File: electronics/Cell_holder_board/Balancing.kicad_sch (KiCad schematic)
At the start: 20 parts, among them Q1 IRLB8721PBF, Q2 IRLB8721PBF, Q3 IRLB8721PBF, Q4 IRLB8721PBF, U3 LTV-817, U4 LTV-817, U5 LTV-817, U6 LTV-817

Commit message: discord session with Johannes and Fabian, Schematic nearly done, all footprints fields filled
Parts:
- removed R17, R18, R19: 100, Resistor_THT:R_Axial_DIN0207_L6.3mm_D2.5mm_P10.16mm_Horizontal, symbol Device:R
- added R20 (x7): 100, Resistor_THT:R_Axial_DIN0207_L6.3mm_D2.5mm_P10.16mm_Horizontal, symbol Device:R
- R21, R22, R23, R24, R25, R26, R27, R28: footprint Resistor_THT:R_Axial_DIN0207_L6.3mm_D2.5mm_P10.16mm_Horizontal -> Resistor_SMD:R_0805_2012Metric
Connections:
- net BT1_+/BT2_-: now also R20.1
- net BT2_+/BT3_-: now also R20.1, R20.1
- net BT3_+/BT4_-: now also R20.1, R20.1
- net BT4_+: now also R20.1, R20.1
- net at Q4.2 (D), R20.2: now also R20.2
- net at Q2.2 (D): now also R20.2, R20.2
- net at Q3.2 (D): now also R20.2, R20.2
- net at Q1.2 (D): now also R20.2, R20.2

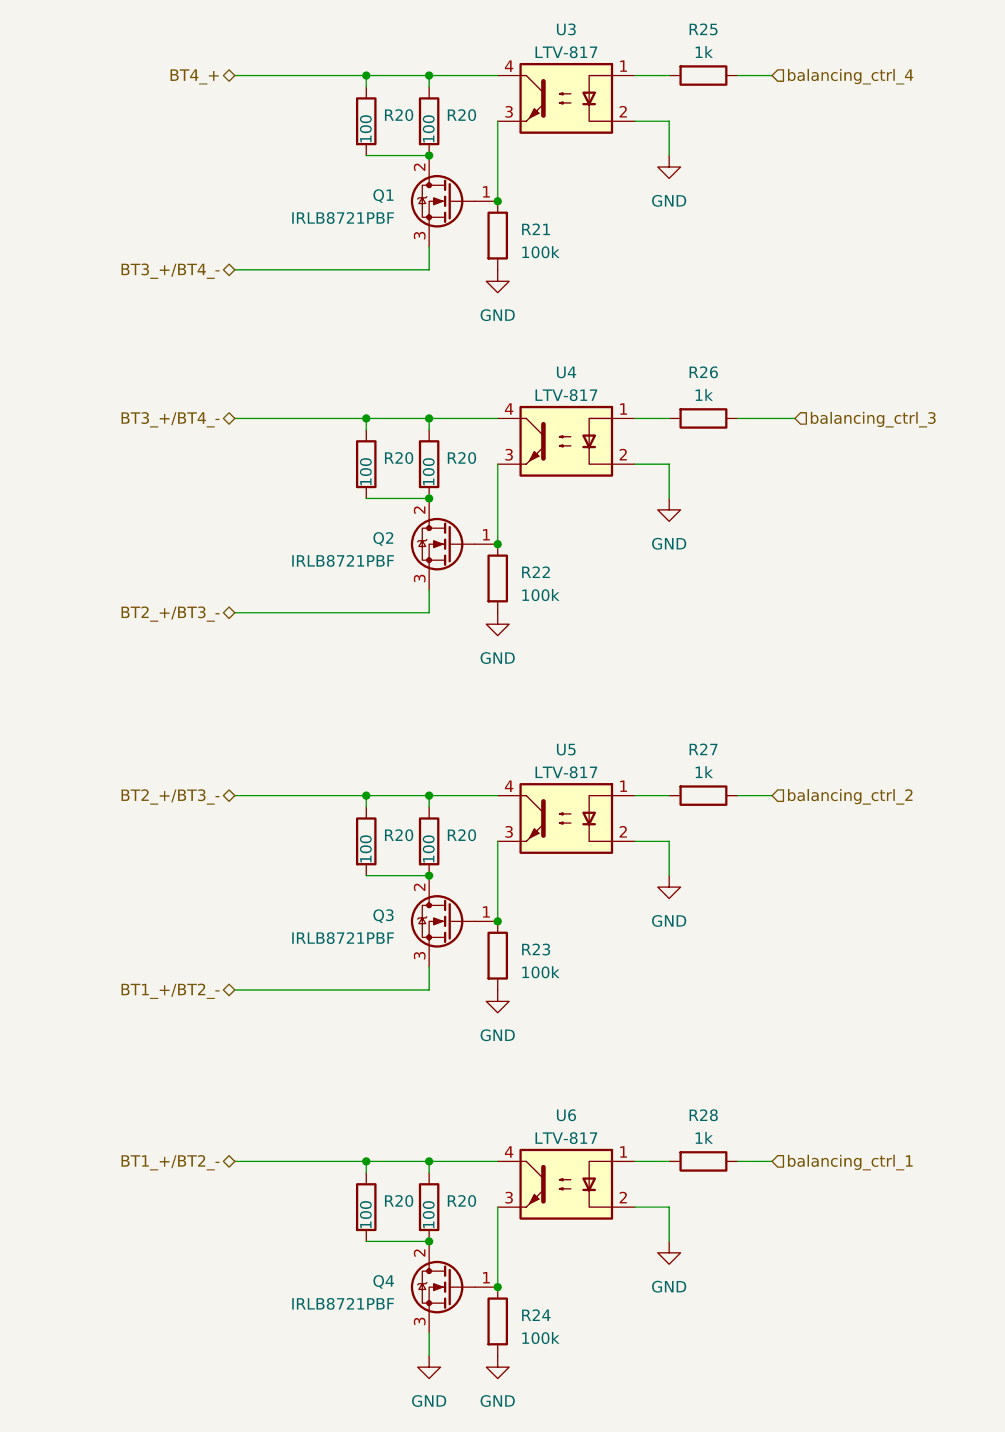
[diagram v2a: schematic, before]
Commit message: finished layout of cell_holder_board
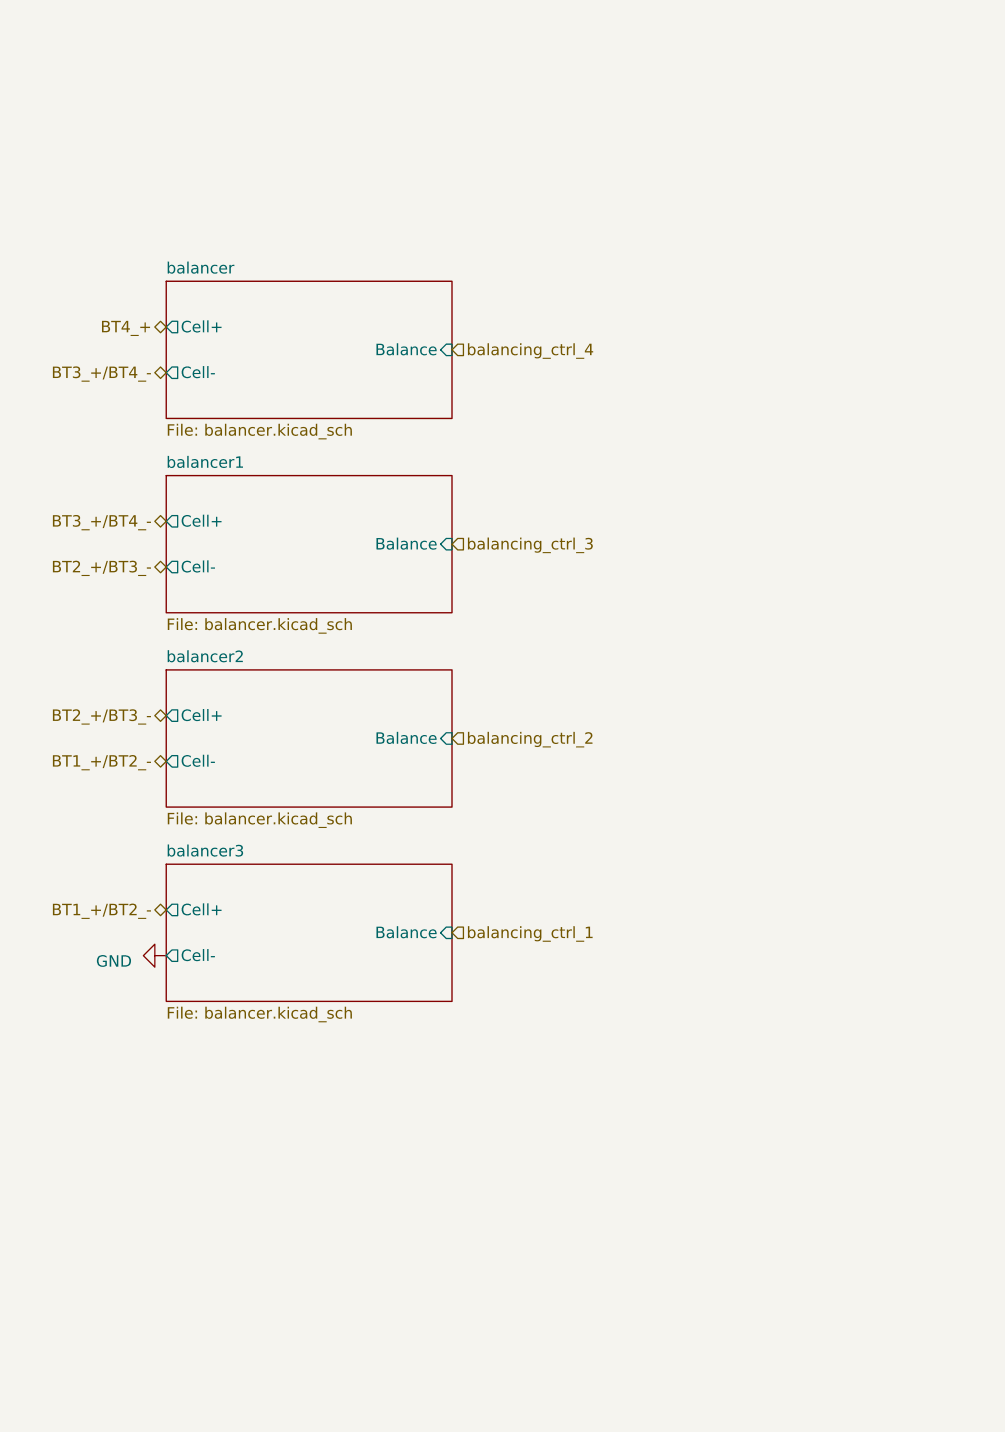
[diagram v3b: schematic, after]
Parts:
- removed Q1, Q2, Q3, Q4: IRLB8721PBF, Package_TO_SOT_THT:TO-220-3_Horizontal_TabDown, symbol Transistor_FET:IRLB8721PBF
- removed R20 (x8): 100, Resistor_THT:R_Axial_DIN0207_L6.3mm_D2.5mm_P10.16mm_Horizontal, symbol Device:R
- removed R21, R22, R23, R24: 100k, Resistor_SMD:R_0805_2012Metric, symbol Device:R
- removed R25, R26, R27, R28: 1k, Resistor_SMD:R_0805_2012Metric, symbol Device:R
- removed U3, U4, U5, U6: LTV-817, Package_DIP:DIP-4_W7.62mm, symbol Isolator:LTV-817
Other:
- added sheet balancer (balancer.kicad_sch)
- added sheet balancer1 (balancer.kicad_sch)
- added sheet balancer2 (balancer.kicad_sch)
- added sheet balancer3 (balancer.kicad_sch)
